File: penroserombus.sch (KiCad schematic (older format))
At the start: 11 parts, among them J1 Conn_01x03_Female, J2 Conn_01x03_Female, J3 Conn_01x03_Male, J4 Conn_01x03_Male, SW1 SW_DPDT_x2

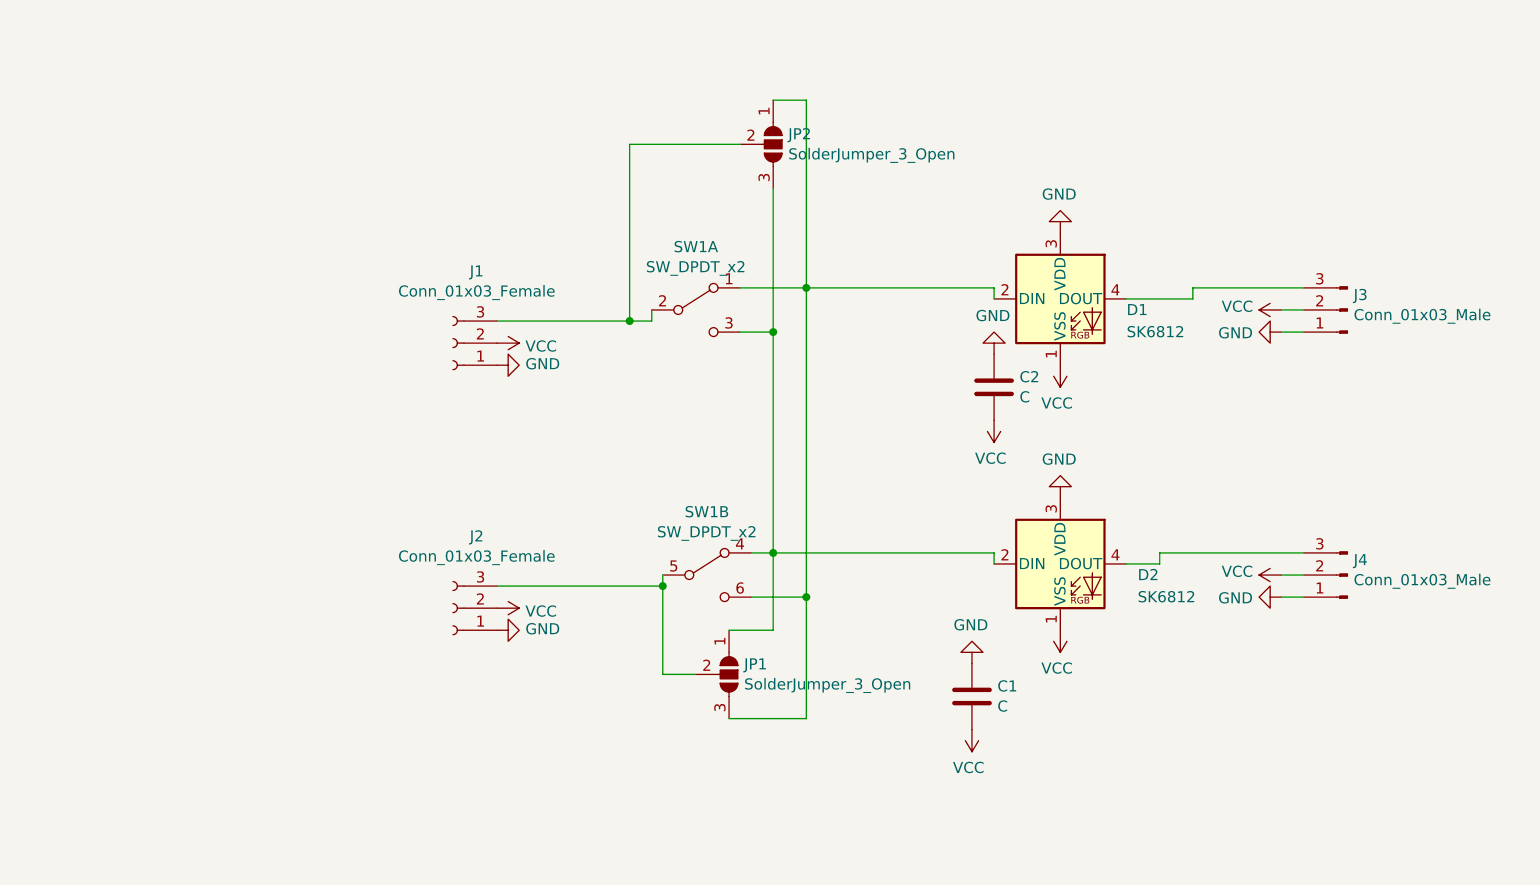
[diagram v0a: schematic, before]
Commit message: made 3535 led version
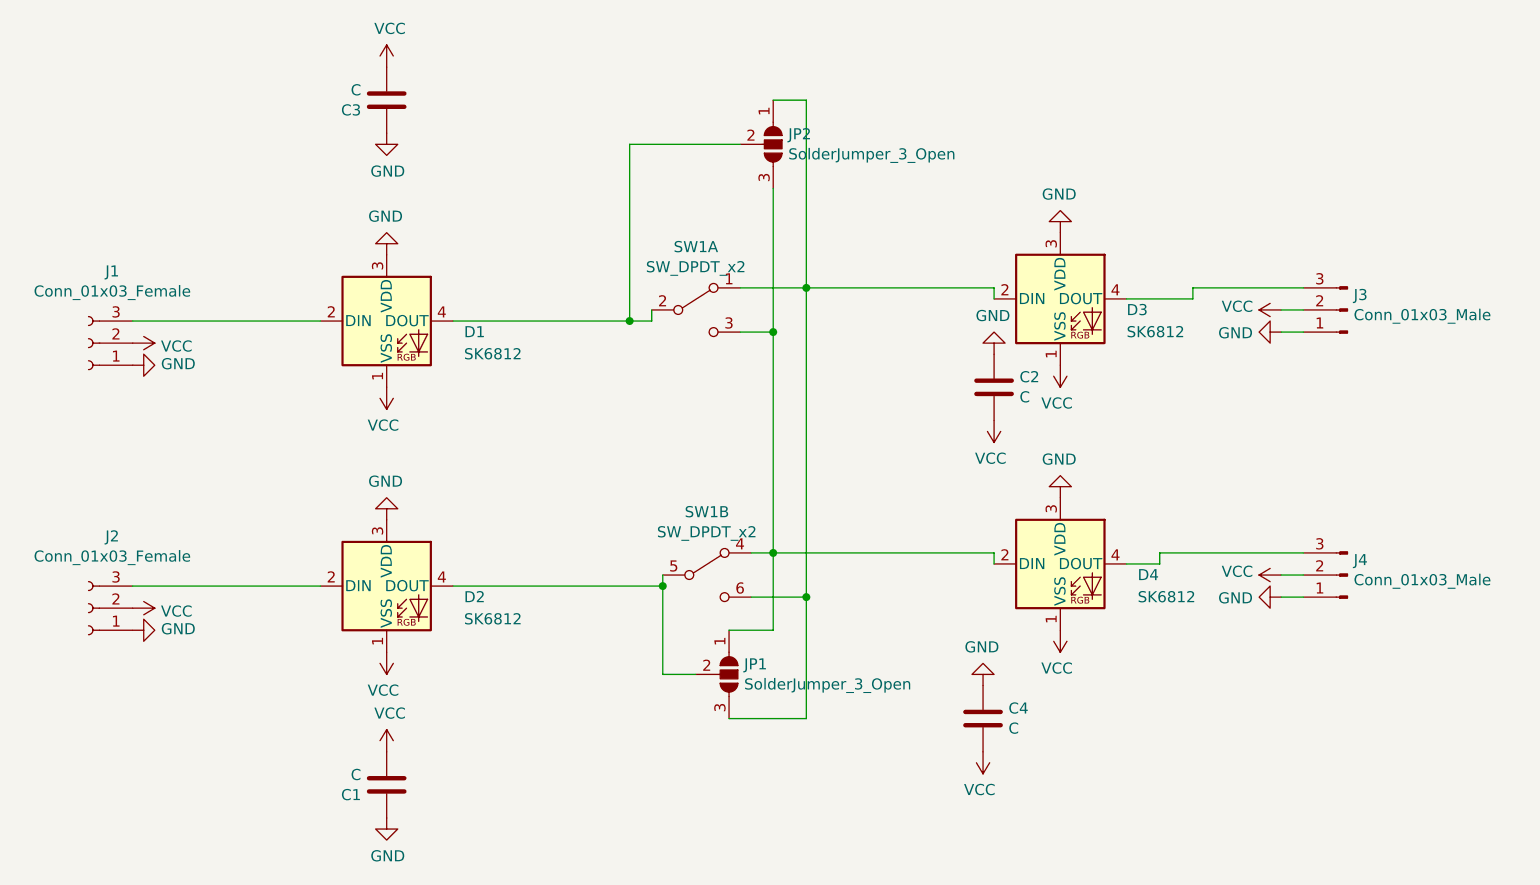
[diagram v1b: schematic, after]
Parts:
- added C3, C4: C, Capacitor_SMD:C_0805_2012Metric_Pad1.18x1.45mm_HandSolder, symbol Device:C
- added D1, D2: SK6812, LED_SMD:LED_SK6812MINI_PLCC4_3.5x3.5mm_P1.75mm, symbol LED:SK6812
- D3: renamed from D1; footprint LED_SMD:LED_SK6812_PLCC4_5.0x5.0mm_P3.2mm -> LED_SMD:LED_SK6812MINI_PLCC4_3.5x3.5mm_P1.75mm
- D4: renamed from D2; footprint LED_SMD:LED_SK6812_PLCC4_5.0x5.0mm_P3.2mm -> LED_SMD:LED_SK6812MINI_PLCC4_3.5x3.5mm_P1.75mm
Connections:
- net GND: now also C3.1, C4.1, D1.3 (VDD), D2.3 (VDD)
- net VCC: now also C3.2, C4.2, D1.1 (VSS), D2.1 (VSS)
- net at JP1.2 (C), SW1.5 (B): now also D2.4 (DOUT); no longer J2.3 (Pin_3)
- net at JP2.2 (C), SW1.2 (B): now also D1.4 (DOUT); no longer J1.3 (Pin_3)
- new net: D2.2 (DIN), J2.3 (Pin_3)
- new net: D1.2 (DIN), J1.3 (Pin_3)
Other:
- moved on the sheet: C1, J1, J2
